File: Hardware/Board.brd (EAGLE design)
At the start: 169.8 x 111.2 mm, 103 parts, among them IC1 BD5229G-TR, IC4 XC6220A331MR-G, J1 FH34SRJ-24S-0.5SH_99_, J2 SAMACSYS_PARTS_USB4110-GF-A, J3 QWIIC_RIGHT_ANGLE, J4 112A-TAAR-R03_ATTEND, Q1 20V/4.2A/52mΩ/1.4W, Q2 20V/4.2A/52mΩ/1.4W, Q3 SI1308EDL-T1-GE3, U1 ESP32_WROVER_SPARKFUN-IC-POWE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, U2 ESP32-C6-WROOM-1-N8, U3 DS3231SN#, U4 MAX17048G+T10, U5 W25Q512JVEIQ

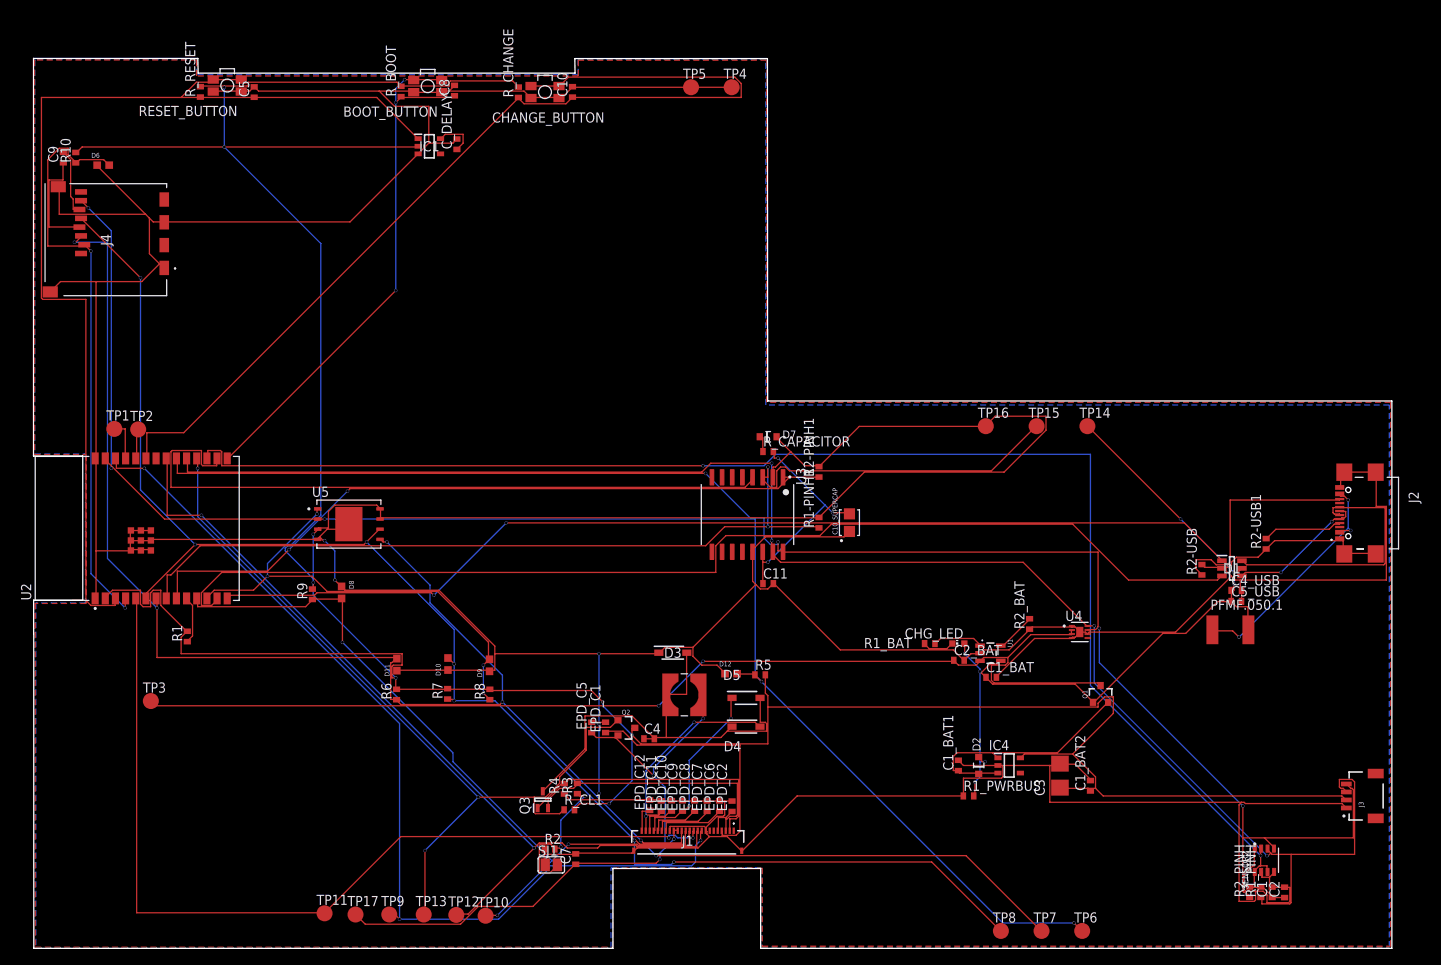
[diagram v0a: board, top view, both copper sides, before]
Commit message: fixed names on board so its readable
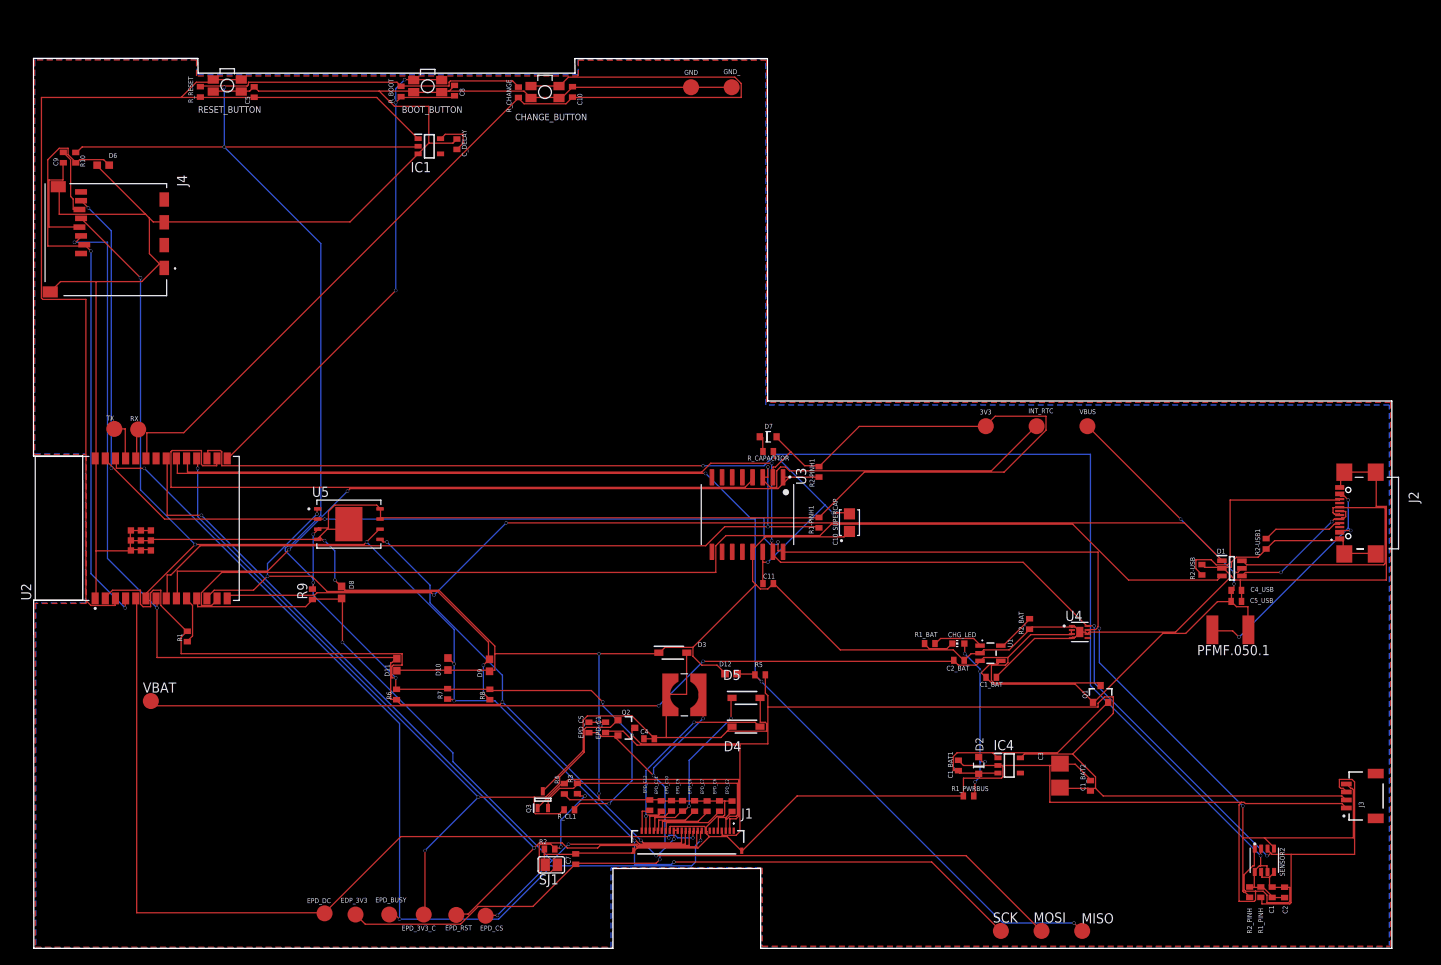
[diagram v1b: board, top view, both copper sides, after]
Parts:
- moved EPD_C5 0.35 mm to (69.4, 27.6)
- renumbered TP1 to TX, TP10 to EPD_CS, TP11 to EPD_DC, TP12 to EPD_RST, TP13 to EPD_3V3_C, TP14 to VBUS, TP15 to INT_RTC, TP16 to 3V3, TP17 to EDP_3V3, TP2 to RX, TP3 to VBAT, TP4 to GND_, TP5 to GND, TP6 to MISO, TP7 to MOSI, TP8 to SCK, TP9 to EPD_BUSY
